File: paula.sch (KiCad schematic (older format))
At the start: 79 parts, among them CN200 DB9P RIGHT(1), CN201 DB9P LEFT(0), CN204 RIGHT AUDIO, CN205 LEFT AUDIO, J200 Conn_01x03_Male, Q200 MPF102, Q201 MPF102, Q202 2N3906, U200 PAULA, U202 74LS157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

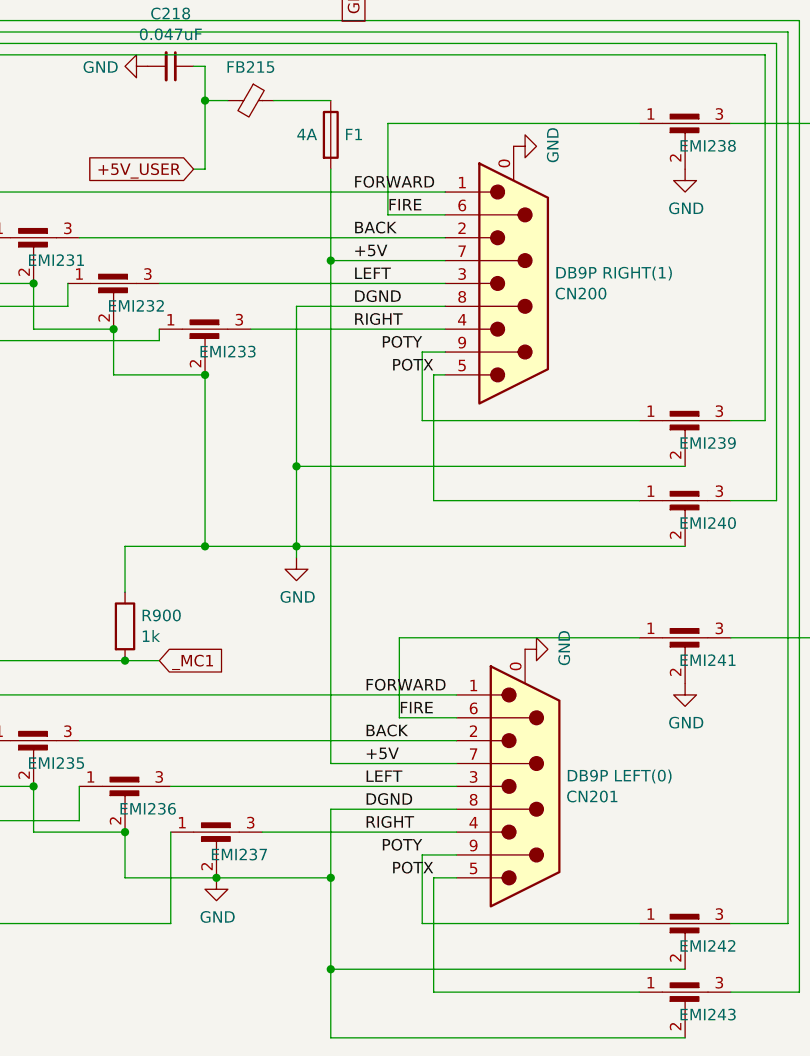
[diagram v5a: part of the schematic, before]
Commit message: Fix joystick ports; Regenerate gerbers and schematics
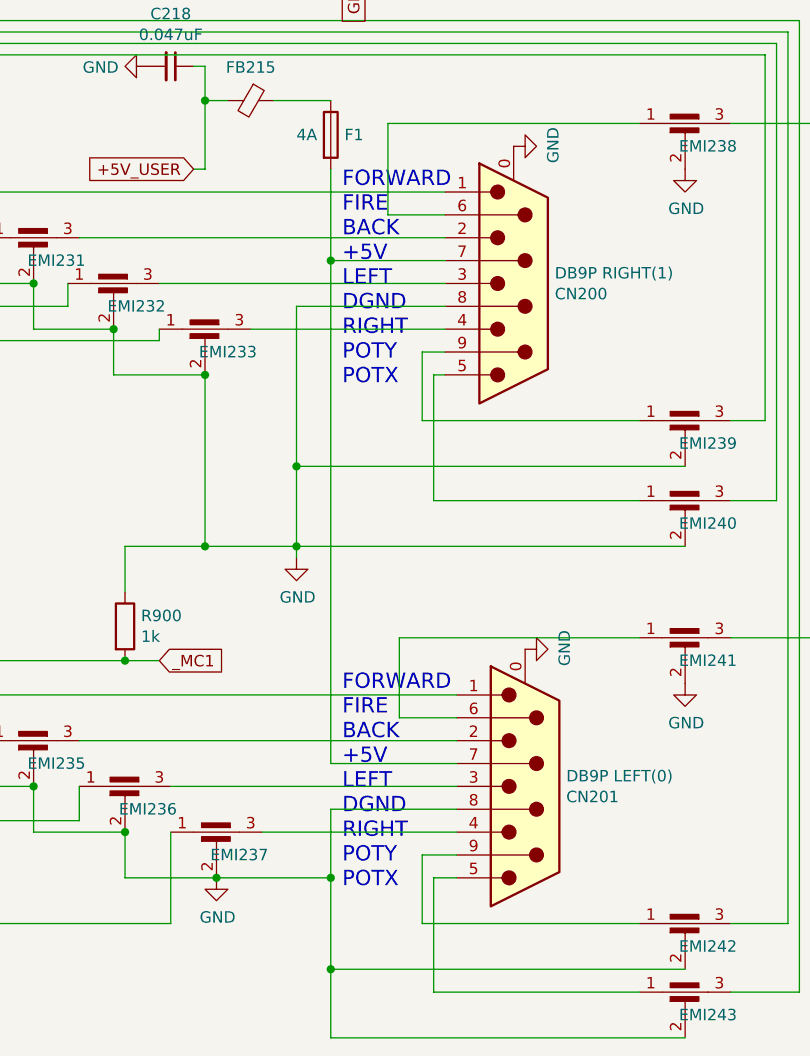
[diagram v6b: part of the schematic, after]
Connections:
- net +5V: no longer CN200.7, CN201.7, F1.2
- net BACK: no longer names the net of CN200.2, EMI231.3
- net BACK: no longer CN201.2, EMI235.3
- net FIRE: no longer names the net of CN200.6, EMI238.1
- net FIRE: no longer CN201.6, EMI241.1
- net FORWARD: no longer names the net of CN200.1, EMI230.3
- net FORWARD: no longer CN201.1, EMI234.3
- net LEFT: no longer names the net of CN200.3, EMI232.3
- net LEFT: no longer CN201.3, EMI236.3
- net POTX: no longer names the net of CN200.5, EMI240.1
- net POTX: no longer CN201.5, EMI243.1
- net POTY: no longer names the net of CN200.9, EMI239.1
- net POTY: no longer CN201.9, EMI242.1
- net RIGHT: no longer names the net of CN200.4, EMI233.3
- net RIGHT: no longer CN201.4, EMI237.3
- new net: CN200.7, CN201.7, F1.2
- new net: CN201.1, EMI234.3
- new net: CN201.2, EMI235.3
- new net: CN201.3, EMI236.3
- new net: CN201.4, EMI237.3
- new net: CN201.5, EMI243.1
- new net: CN201.6, EMI241.1
- new net: CN201.9, EMI242.1
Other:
- note added: "FORWARD\nFIRE\nBACK\n+5V\nLEFT\nDGND\nRIGHT\nPOTY\nPOTX"
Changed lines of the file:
@@
 EESchema Schematic File Version 4
-LIBS:amiga2000-cache
-EELAYER 29 0
+EELAYER 30 0
 EELAYER END
 $Descr A3 16535 11693
@@
 Wire Wire Line
 	3800 5050 3350 5050
-Text Label 7750 7300 0    50   ~ 0
-FORWARD
-Text Label 7750 7500 0    50   ~ 0
-BACK
-Text Label 7750 7700 0    50   ~ 0
-LEFT
-Text Label 7750 7900 0    50   ~ 0
-RIGHT
-Text Label 7900 7400 0    50   ~ 0
-FIRE
 Wire Wire Line
 	8150 7600 7650 7600
@@
 Wire Wire Line
 	8150 7800 7500 7800
-Text Label 7750 7600 0    50   ~ 0
-+5V
-Text Label 7750 7800 0    50   ~ 0
-DGND
-Text Label 8050 8000 2    50   ~ 0
-POTY
-Text Label 8100 8100 2    50   ~ 0
-POTX
 $Comp
 L Connector:DB9_Male_MountingHoles CN201
@@
 	1    0    0    1
 $EndComp
-Text Label 7800 9500 0    50   ~ 0
-FORWARD
-Text Label 7800 9700 0    50   ~ 0
-BACK
-Text Label 7800 9900 0    50   ~ 0
-LEFT
-Text Label 7800 10100 0    50   ~ 0
-RIGHT
-Text Label 7950 9600 0    50   ~ 0
-FIRE
-Text Label 7800 9800 0    50   ~ 0
-+5V
-Text Label 7800 10000 0    50   ~ 0
-DGND
-Text Label 8050 10200 2    50   ~ 0
-POTY
-Text Label 8100 10300 2    50   ~ 0
-POTX
 Wire Wire Line
 	7650 7600 7650 9800
@@
 Wire Bus Line
 	1300 1800 1300 3300
+Text Notes 7700 8150 0    67   ~ 0
+FORWARD\nFIRE\nBACK\n+5V\nLEFT\nDGND\nRIGHT\nPOTY\nPOTX
+Text Notes 7700 10350 0    67   ~ 0
+FORWARD\nFIRE\nBACK\n+5V\nLEFT\nDGND\nRIGHT\nPOTY\nPOTX
 $EndSCHEMATC
